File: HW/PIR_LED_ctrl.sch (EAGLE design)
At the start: 3 parts, among them J1 POWER_JACKPTH

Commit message: added brd file
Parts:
- added C1, C2: (no value), rcl:C-EUC1206
- added U1: (no value), pero_library:LM36713.3V
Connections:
- new net N$2: C2.2, U1.OUT
- net 12V: now also C1.2, U1.EN, U1.IN
- net GND: now also C1.1, C2.1, U1.GND
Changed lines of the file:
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@@
 <part name="P+1" library="supply1" deviceset="VCC" device="" value="12V"/>
 <part name="P+2" library="supply1" deviceset="VCC" device="" value="5V"/>
+<part name="U1" library="pero_library" deviceset="LM3671" device="3.3V"/>
+<part name="GND4" library="supply1" deviceset="GND" device=""/>
+<part name="C1" library="rcl" deviceset="C-EU" device="C1206"/>
+<part name="C2" library="rcl" deviceset="C-EU" device="C1206"/>
 </parts>
 <sheets>
@@
 <instance part="P+1" gate="VCC" x="-33.02" y="27.94"/>
 <instance part="P+2" gate="VCC" x="17.78" y="-5.08"/>
+<instance part="U1" gate="G$1" x="-7.62" y="17.78"/>
+<instance part="GND4" gate="1" x="-20.32" y="5.08"/>
+<instance part="C1" gate="G$1" x="-25.4" y="12.7" rot="R180"/>
+<instance part="C2" gate="G$1" x="25.4" y="15.24" rot="R180"/>
 </instances>
 <busses>
@@
 <segment>
 <pinref part="GND3" gate="1" pin="GND"/>
-<wire x1="-45.72" y1="17.78" x2="-30.48" y2="17.78" width="0.1524" layer="91"/>
 <pinref part="J1" gate="G$1" pin="GND"/>
 <wire x1="-48.26" y1="17.78" x2="-45.72" y2="17.78" width="0.1524" layer="91"/>
@@
 <wire x1="-45.72" y1="20.32" x2="-45.72" y2="17.78" width="0.1524" layer="91"/>
 <junction x="-45.72" y="17.78"/>
+</segment>
+<segment>
+<pinref part="U1" gate="G$1" pin="GND"/>
+<pinref part="GND4" gate="1" pin="GND"/>
+<wire x1="-17.78" y1="12.7" x2="-20.32" y2="12.7" width="0.1524" layer="91"/>
+<wire x1="-20.32" y1="12.7" x2="-20.32" y2="7.62" width="0.1524" layer="91"/>
+<pinref part="C1" gate="G$1" pin="1"/>
+<wire x1="-25.4" y1="10.16" x2="-25.4" y2="7.62" width="0.1524" layer="91"/>
+<wire x1="-25.4" y1="7.62" x2="-20.32" y2="7.62" width="0.1524" layer="91"/>
+<pinref part="C2" gate="G$1" pin="1"/>
+<wire x1="-20.32" y1="7.62" x2="25.4" y2="7.62" width="0.1524" layer="91"/>
+<wire x1="25.4" y1="7.62" x2="25.4" y2="12.7" width="0.1524" layer="91"/>
+<junction x="-20.32" y="7.62"/>
 </segment>
 </net>
@@
 <wire x1="-33.02" y1="22.86" x2="-33.02" y2="25.4" width="0.1524" layer="91"/>
 <pinref part="P+1" gate="VCC" pin="VCC"/>
+<pinref part="U1" gate="G$1" pin="IN"/>
+<wire x1="-33.02" y1="22.86" x2="-25.4" y2="22.86" width="0.1524" layer="91"/>
+<pinref part="U1" gate="G$1" pin="EN"/>
+<wire x1="-25.4" y1="22.86" x2="-20.32" y2="22.86" width="0.1524" layer="91"/>
+<wire x1="-20.32" y1="22.86" x2="-17.78" y2="22.86" width="0.1524" layer="91"/>
+<wire x1="-17.78" y1="17.78" x2="-20.32" y2="17.78" width="0.1524" layer="91"/>
+<wire x1="-20.32" y1="17.78" x2="-20.32" y2="22.86" width="0.1524" layer="91"/>
+<junction x="-33.02" y="22.86"/>
+<pinref part="C1" gate="G$1" pin="2"/>
+<wire x1="-25.4" y1="17.78" x2="-25.4" y2="22.86" width="0.1524" layer="91"/>
+<junction x="-25.4" y="22.86"/>
+<junction x="-20.32" y="22.86"/>
 </segment>
 </net>
@@
 </segment>
 </net>
+<net name="N$2" class="0">
+<segment>
+<pinref part="U1" gate="G$1" pin="OUT"/>
+<pinref part="C2" gate="G$1" pin="2"/>
+<wire x1="0" y1="22.86" x2="25.4" y2="22.86" width="0.1524" layer="91"/>
+<wire x1="25.4" y1="22.86" x2="25.4" y2="20.32" width="0.1524" layer="91"/>
+</segment>
+</net>

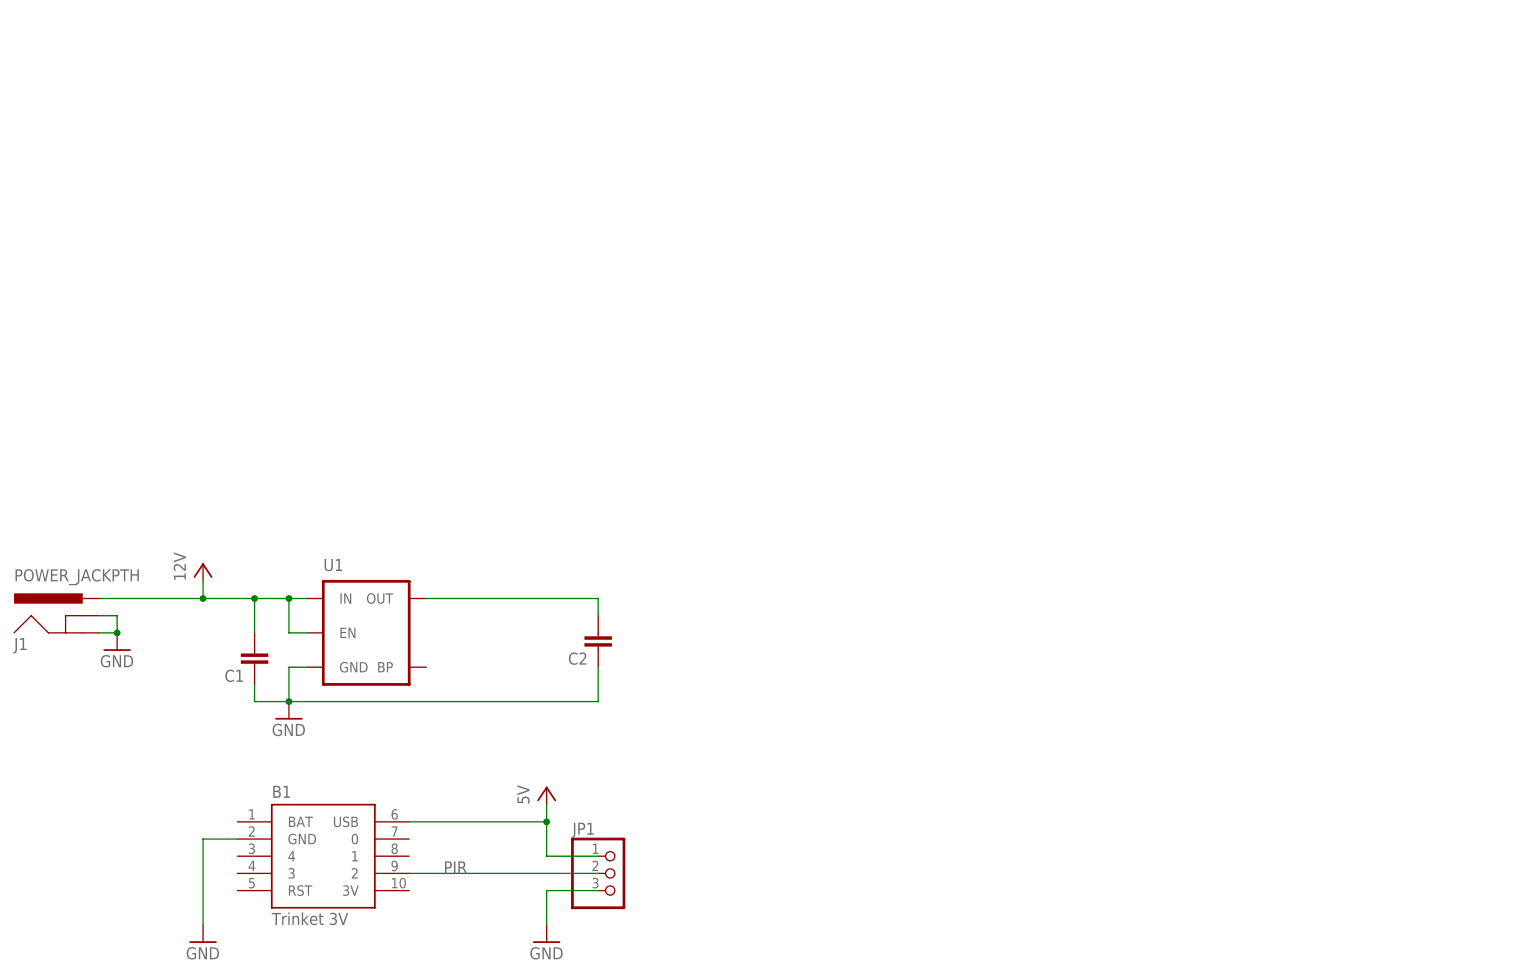
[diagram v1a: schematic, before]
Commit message: added holes and released everything
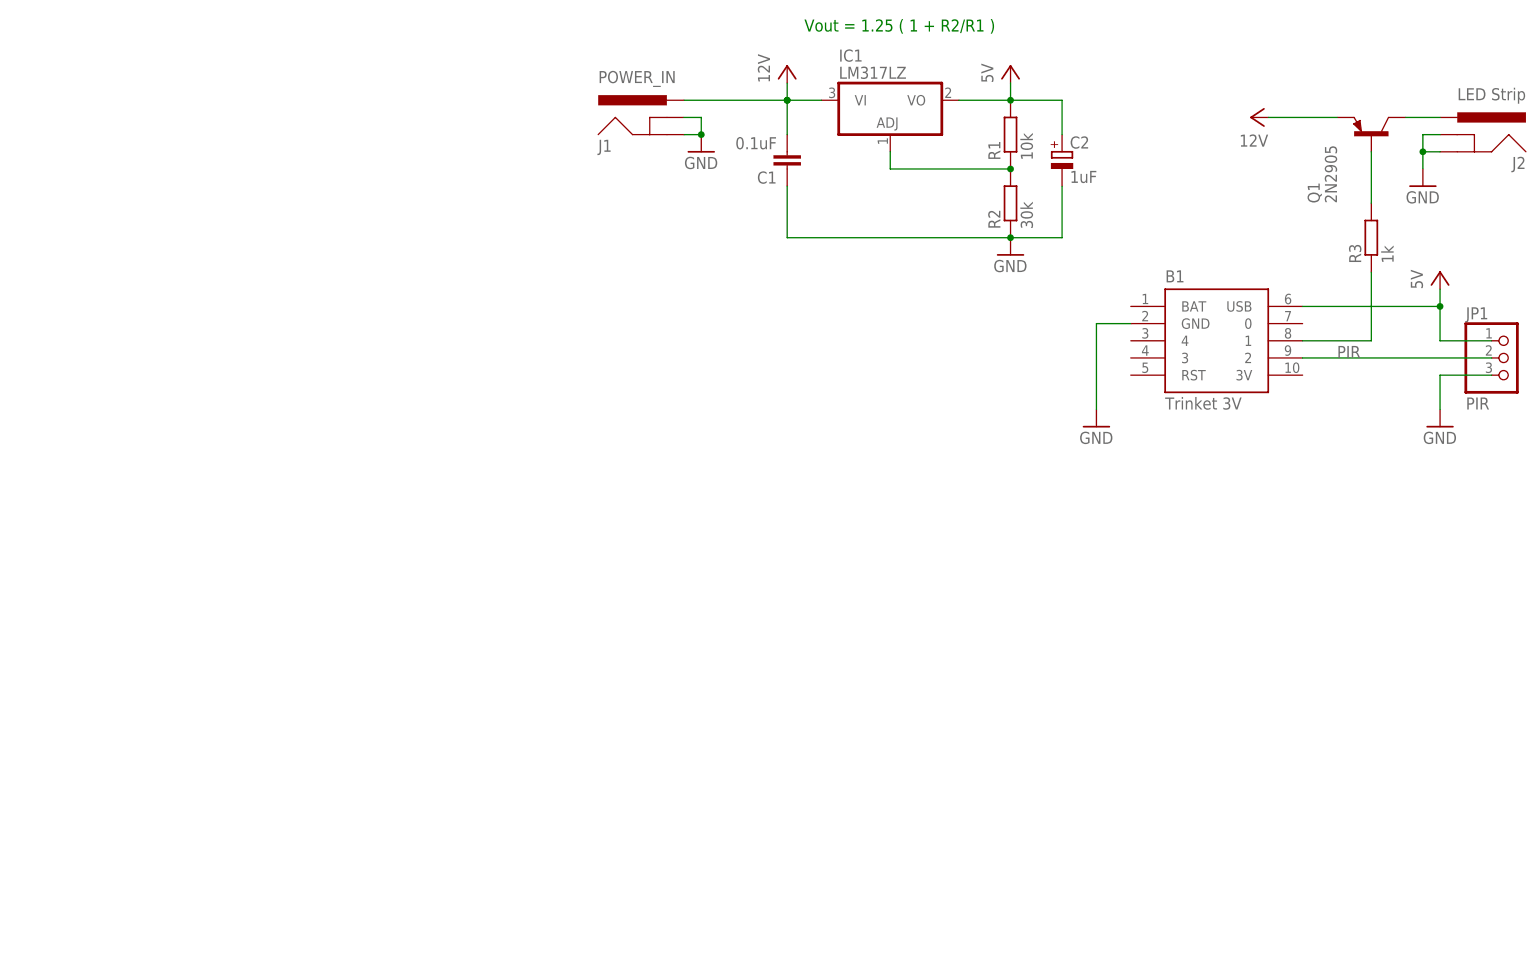
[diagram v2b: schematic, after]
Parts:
- removed U1: (no value), pero_library:LM36713.3V
- added IC1: LM317LZ, linear:LM317LZ
- added J2: LED Strip, SparkFun-Connectors:POWER_JACKPTH
- added Q1: 2N2905, transistor:2N2905-PNP-TO39-EBC
- added R1: 10k, rcl:R-EU_0207/10
- added R2: 30k, rcl:R-EU_0207/10
- added R3: 1k, rcl:R-EU_0207/10
- C1: value (none) -> 0.1uF; device rcl:C-EUC1206 -> rcl:C-EU025-025X050
- C2: value (none) -> 1uF; device rcl:C-EUC1206 -> rcl:CPOL-EUE5-6
- J1: value POWER_JACKPTH -> POWER_IN
- JP1: value (none) -> PIR
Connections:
- new net N$1: IC1.ADJ, R1.1, R2.2
- new net N$3: B1.1, R3.1
- new net N$4: Q1.B, R3.2
- net 12V: now also IC1.VI, Q1.E; no longer U1.EN, U1.IN
- net 5V: now also C2.+, IC1.VO, R1.2
- net GND: now also C2.-, J2.GND, J2.GNDBREAK, R2.1; no longer C2.1, U1.GND
- net N$2: now also J2.PWR, Q1.C; no longer C2.2, U1.OUT
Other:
- note added: "Vout = 1.25 ( 1 + R2/R1 )"
- moved on the sheet: B1, C1, J1, JP1
